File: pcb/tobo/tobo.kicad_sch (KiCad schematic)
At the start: 94 parts, among them J1 Molex 538-54548-2272, J2 Conn_01x02_Pin, J4 Molex 538-54548-2472, J5 Conn_01x09_Pin, J6 Conn_01x09_Pin, J7 Conn_01x09_Pin, J8 Hroparts Elec TYPE-C-31-M-12, U1 TS5A23167, U10 5015, U11 5015, U12 5015, U13 5015, U14 CH340E, U15 5015, U2 ATmega328P-A, U3 TS5A23167, U4 TS5A23167, U5 TS5A23167, U6 5015, U7 5015, U8 5015, U9 5015, X7 TestPoint, Y4 TestPoint

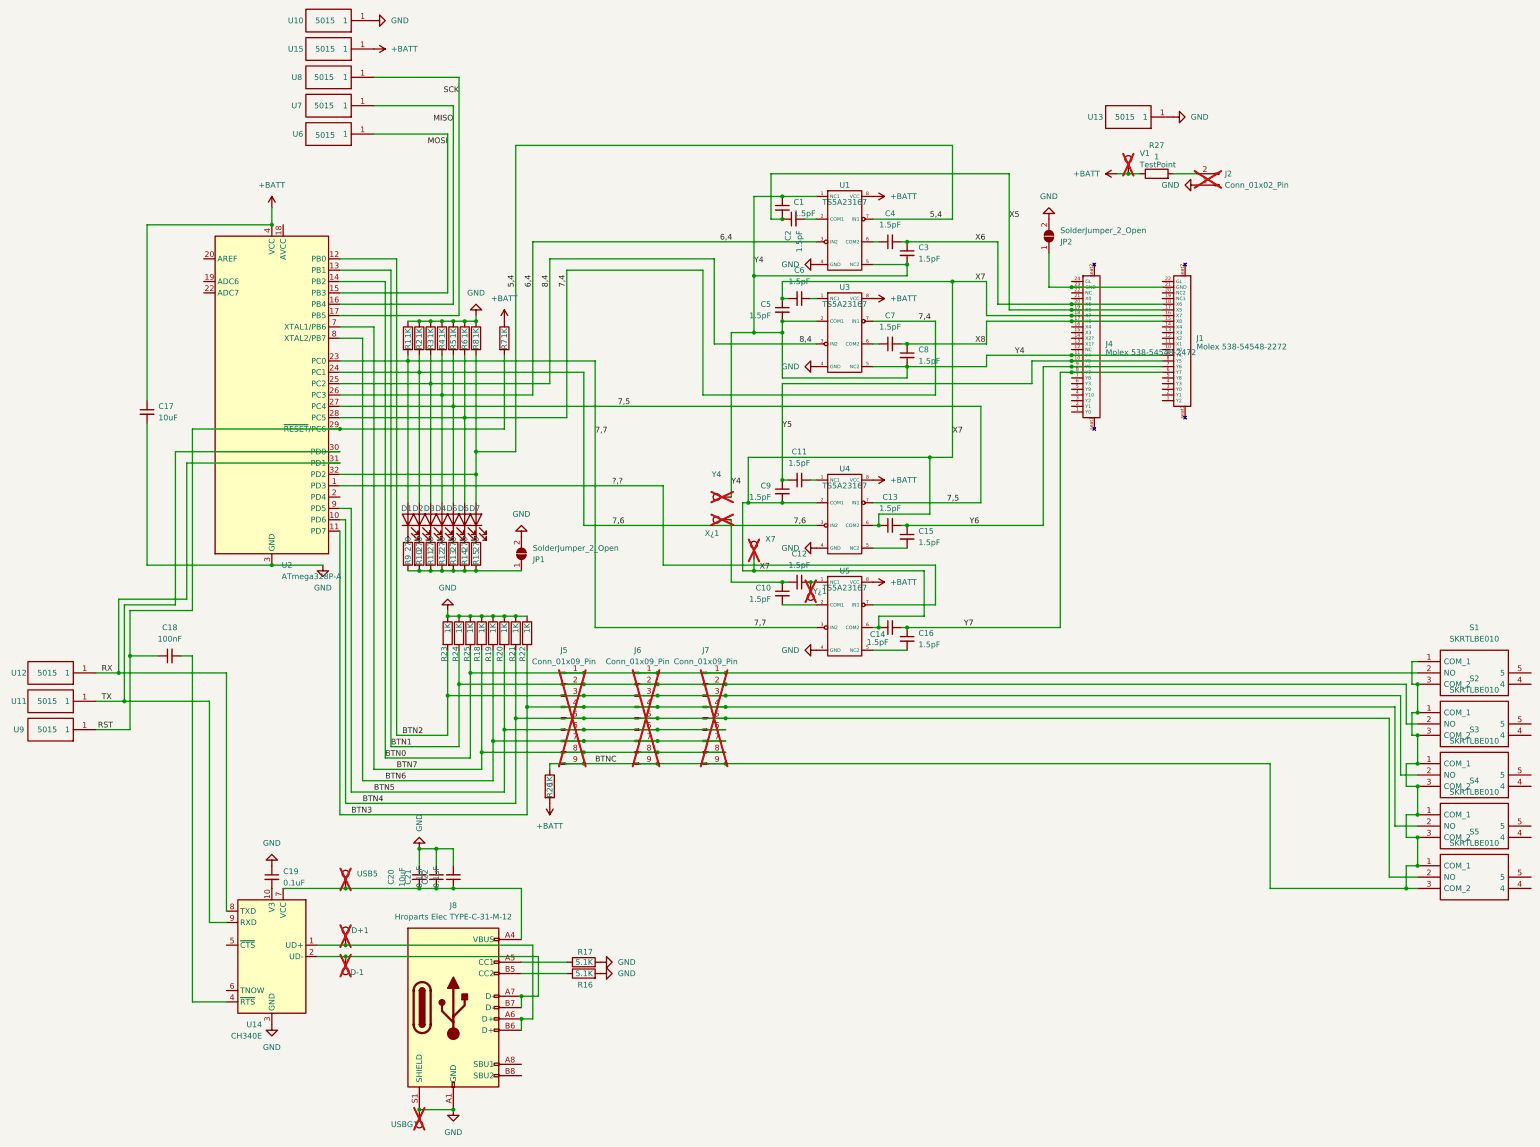
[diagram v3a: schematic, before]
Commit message: PCB cleanup, RST connector clarification
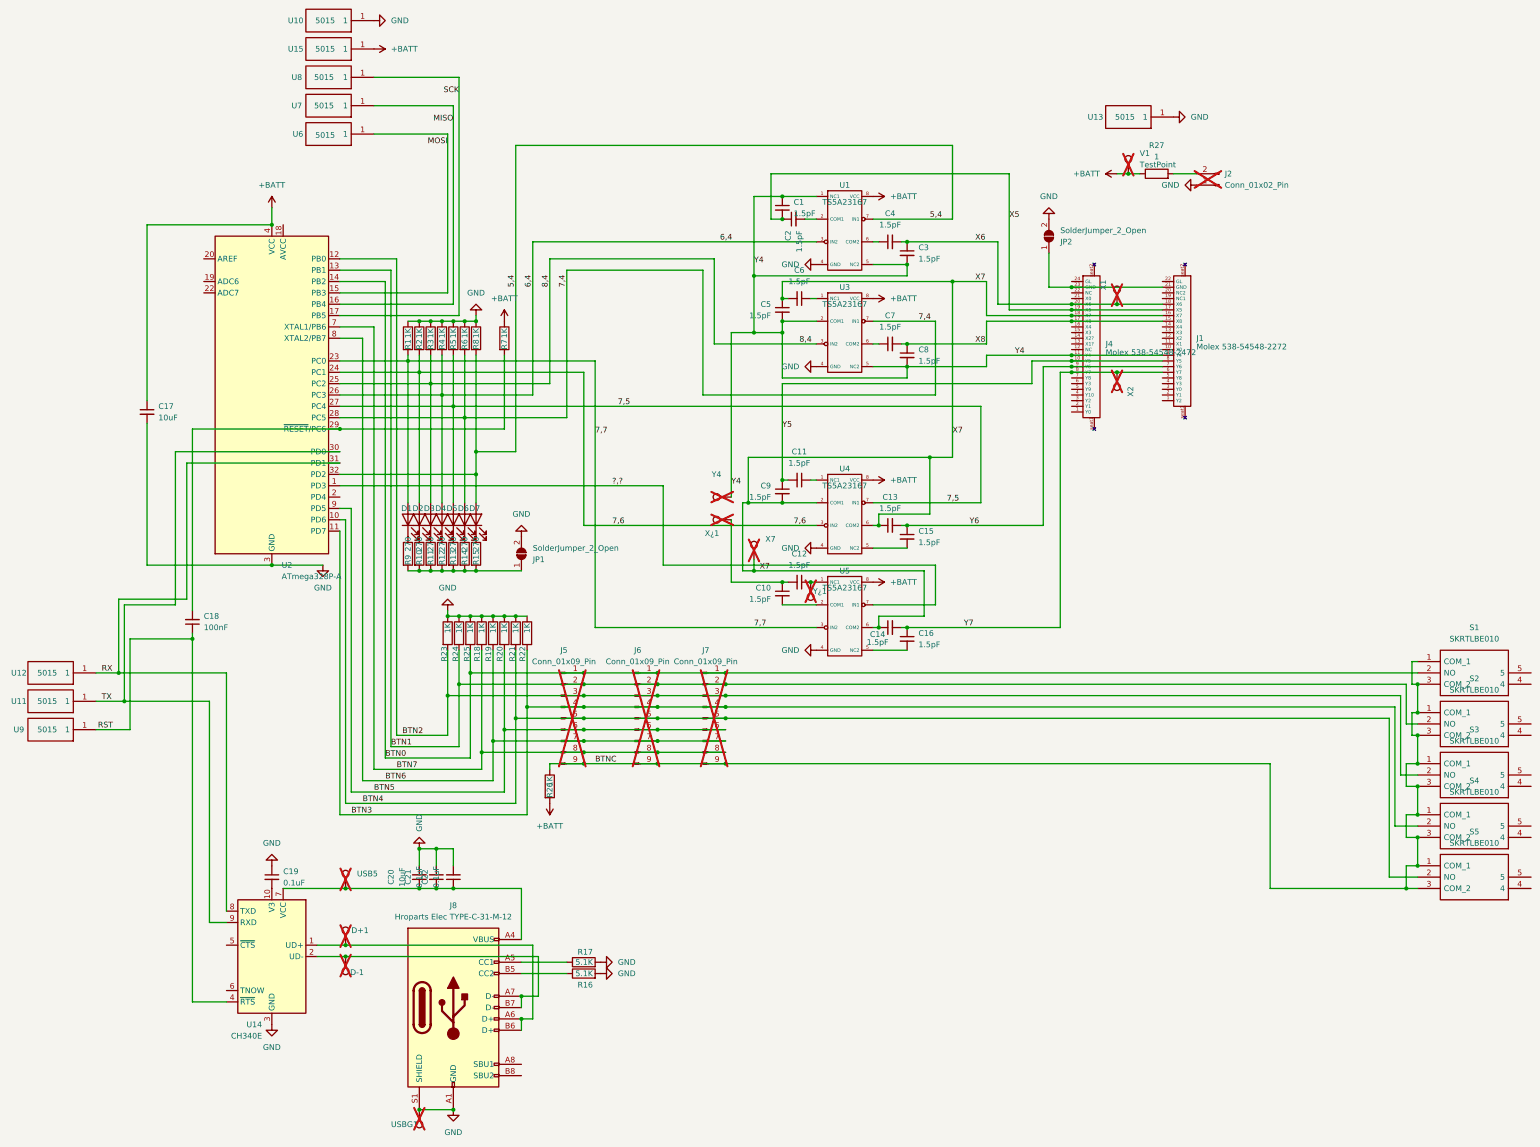
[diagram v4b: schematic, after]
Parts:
- added X1, X2: TestPoint, TestPoint:TestPoint_Pad_D1.0mm, symbol Connector:TestPoint
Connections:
- net RST: now also U14.4 (~{RTS}); no longer R7.2, U2.29 (~{RESET}/PC6)
- net X6: now also X1.1
- net Y7: now also X2.1
- net at C18.2: now also R7.2, U2.29 (~{RESET}/PC6); no longer U14.4 (~{RTS})
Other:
- moved on the sheet: C18
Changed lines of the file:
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@@
 	)
 	(junction
+		(at 264.16 97.79)
+		(diameter 0)
+		(color 0 0 0 0)
+	)
+	(junction
 		(at 176.53 175.26)
 		(diameter 0)
@@
 	)
 	(junction
-		(at 43.18 161.29)
-		(diameter 0)
-		(color 0 0 0 0)
-	)
-	(junction
 		(at 331.47 201.93)
 		(diameter 0)
@@
 	)
 	(junction
+		(at 57.15 157.48)
+		(diameter 0)
+		(color 0 0 0 0)
+	)
+	(junction
 		(at 130.81 237.49)
 		(diameter 0)
@@
 	)
 	(junction
+		(at 264.16 82.55)
+		(diameter 0)
+		(color 0 0 0 0)
+	)
+	(junction
 		(at 189.23 58.42)
 		(diameter 0)
@@
 	(wire
 		(pts
-			(xy 274.32 93.98) (xy 254 93.98)
-		)
-		(stroke
-			(width 0)
-			(type default)
-		)
-	)
-	(wire
-		(pts
-			(xy 43.18 161.29) (xy 43.18 177.8)
-		)
-		(stroke
-			(width 0)
-			(type default)
-		)
-	)
-	(wire
-		(pts
 			(xy 133.35 102.87) (xy 113.03 102.87)
 		)
@@
 	(wire
 		(pts
-			(xy 43.18 151.13) (xy 57.15 151.13)
-		)
-		(stroke
-			(width 0)
-			(type default)
-		)
-	)
-	(wire
-		(pts
 			(xy 328.93 176.53) (xy 331.47 176.53)
 		)
@@
 	(wire
 		(pts
+			(xy 264.16 82.55) (xy 254 82.55)
+		)
+		(stroke
+			(width 0)
+			(type default)
+		)
+	)
+	(wire
+		(pts
 			(xy 248.92 78.74) (xy 254 78.74)
 		)
@@
 	(wire
 		(pts
-			(xy 274.32 97.79) (xy 254 97.79)
+			(xy 274.32 97.79) (xy 264.16 97.79)
 		)
 		(stroke
@@
 	(wire
 		(pts
+			(xy 57.15 157.48) (xy 57.15 238.76)
+		)
+		(stroke
+			(width 0)
+			(type default)
+		)
+	)
+	(wire
+		(pts
 			(xy 130.81 242.57) (xy 133.35 242.57)
 		)
@@
 	(wire
 		(pts
-			(xy 274.32 82.55) (xy 254 82.55)
+			(xy 274.32 82.55) (xy 264.16 82.55)
 		)
 		(stroke
@@
 	(wire
 		(pts
+			(xy 43.18 157.48) (xy 57.15 157.48)
+		)
+		(stroke
+			(width 0)
+			(type default)
+		)
+	)
+	(wire
+		(pts
 			(xy 90.17 90.17) (xy 95.25 90.17)
 		)
@@
 	(wire
 		(pts
+			(xy 254 93.98) (xy 274.32 93.98)
+		)
+		(stroke
+			(width 0)
+			(type default)
+		)
+	)
+	(wire
+		(pts
 			(xy 107.95 208.28) (xy 107.95 204.47)
 		)
@@
 	(wire
 		(pts
+			(xy 43.18 157.48) (xy 43.18 177.8)
+		)
+		(stroke
+			(width 0)
+			(type default)
+		)
+	)
+	(wire
+		(pts
 			(xy 120.65 120.65) (xy 120.65 115.57)
 		)
@@
 	(wire
 		(pts
-			(xy 43.18 161.29) (xy 49.53 161.29)
-		)
-		(stroke
-			(width 0)
-			(type default)
-		)
-	)
-	(wire
-		(pts
-			(xy 57.15 161.29) (xy 57.15 238.76)
+			(xy 57.15 156.21) (xy 57.15 157.48)
 		)
 		(stroke
@@
 	(wire
 		(pts
-			(xy 57.15 161.29) (xy 54.61 161.29)
-		)
-		(stroke
-			(width 0)
-			(type default)
-		)
-	)
-	(wire
-		(pts
 			(xy 120.65 142.24) (xy 130.81 142.24)
 		)
@@
 	(wire
 		(pts
-			(xy 43.18 151.13) (xy 43.18 161.29)
+			(xy 189.23 121.92) (xy 190.5 121.92)
 		)
 		(stroke
@@
 	(wire
 		(pts
-			(xy 189.23 121.92) (xy 190.5 121.92)
+			(xy 264.16 53.34) (xy 266.7 53.34)
 		)
 		(stroke
@@
 	(wire
 		(pts
-			(xy 264.16 53.34) (xy 266.7 53.34)
+			(xy 227.33 77.47) (xy 234.95 77.47)
 		)
 		(stroke
@@
 	(wire
 		(pts
-			(xy 227.33 77.47) (xy 234.95 77.47)
+			(xy 245.11 95.25) (xy 245.11 100.33)
 		)
 		(stroke
@@
 	(wire
 		(pts
-			(xy 245.11 95.25) (xy 245.11 100.33)
+			(xy 274.32 96.52) (xy 254 96.52)
 		)
 		(stroke
@@
 	(wire
 		(pts
-			(xy 274.32 96.52) (xy 254 96.52)
+			(xy 140.97 74.93) (xy 140.97 107.95)
 		)
 		(stroke
@@
 	(wire
 		(pts
-			(xy 140.97 74.93) (xy 140.97 107.95)
+			(xy 264.16 97.79) (xy 254 97.79)
 		)
 		(stroke
@@
 	)
 	(symbol
+		(lib_id "Connector:TestPoint")
+		(at 264.16 97.79 180)
+		(unit 1)
+		(exclude_from_sim no)
+		(in_bom no)
+		(on_board yes)
+		(dnp yes)
+		(property "Reference" "X2"
+			(at 267.208 102.108 90)
+			(effects
+				(font
+					(size 1.27 1.27)
+				)
+			)
+		)
+		(property "Value" "TestPoint"
+			(at 261.62 101.092 90)
+			(effects
+				(font
+					(size 1.27 1.27)
+				)
+				(hide yes)
+			)
+		)
+		(property "Footprint" "TestPoint:TestPoint_Pad_D1.0mm"
+			(at 259.08 97.79 0)
+			(effects
+				(font
+					(size 1.27 1.27)
+				)
+				(hide yes)
+			)
+		)
+		(property "Datasheet" "~"
+			(at 259.08 97.79 0)
+			(effects
+				(font
+					(size 1.27 1.27)
+				)
+				(hide yes)
+			)
+		)
+		(property "Description" "test point"
+			(at 264.16 97.79 0)
+			(effects
+				(font
+					(size 1.27 1.27)
+				)
+				(hide yes)
+			)
+		)
+		(pin "1"
+		)
+		(instances
+			(project "tobo"
+				(path "/ce2fc4a9-618f-4cc1-898a-224ffa79d770"
+					(reference "X2")
+					(unit 1)
+				)
+			)
+		)
+	)
+	(symbol
 		(lib_id "Device:R")
 		(at 110.49 138.43 0)
@@
 	(symbol
 		(lib_id "Device:C_Small")
-		(at 52.07 161.29 90)
+		(at 57.15 153.67 180)
 		(unit 1)
 		(exclude_from_sim no)
@@
 		(fields_autoplaced yes)
 		(property "Reference" "C18"
-			(at 52.0763 154.94 90)
+			(at 59.69 152.3935 0)
 			(effects
 				(font
 					(size 1.27 1.27)
 				)
+				(justify right)
 			)
 		)
 		(property "Value" "100nF"
-			(at 52.0763 157.48 90)
+			(at 59.69 154.9335 0)
 			(effects
 				(font
 					(size 1.27 1.27)
 				)
+				(justify right)
 			)
 		)
 		(property "Footprint" "Capacitor_SMD:C_0201_0603Metric"
-			(at 52.07 161.29 0)
+			(at 57.15 153.67 0)
 			(effects
 				(font
@@
 		)
 		(property "Datasheet" "~"
-			(at 52.07 161.29 0)
+			(at 57.15 153.67 0)
 			(effects
 				(font
@@
 		)
 		(property "Description" "Unpolarized capacitor, small symbol"
-			(at 52.07 161.29 0)
+			(at 57.15 153.67 0)
 			(effects
 				(font
@@
 					(unit 1)
 				)
+			)
+		)
+	)
+	(symbol
+		(lib_id "Connector:TestPoint")
+		(at 264.16 82.55 0)
+		(unit 1)
+		(exclude_from_sim no)
+		(in_bom no)
+		(on_board yes)
+		(dnp yes)
+		(property "Reference" "X1"
+			(at 261.112 78.232 90)
+			(effects
+				(font
+					(size 1.27 1.27)
+				)
+			)
+		)
+		(property "Value" "TestPoint"
+			(at 266.7 79.248 90)
+			(effects
+				(font
+					(size 1.27 1.27)
+				)
+				(hide yes)
+			)
+		)
+		(property "Footprint" "TestPoint:TestPoint_Pad_D1.0mm"
+			(at 269.24 82.55 0)
+			(effects
+				(font
+					(size 1.27 1.27)
+				)
+				(hide yes)
+			)
+		)
+		(property "Datasheet" "~"
+			(at 269.24 82.55 0)
+			(effects
+				(font
+					(size 1.27 1.27)
+				)
+				(hide yes)
+			)
+		)
+		(property "Description" "test point"
+			(at 264.16 82.55 0)
+			(effects
+				(font
+					(size 1.27 1.27)
+				)
+				(hide yes)
+			)
+		)
+		(pin "1"
+		)
+		(instances
+			(project "tobo"
+				(path "/ce2fc4a9-618f-4cc1-898a-224ffa79d770"
+					(reference "X1")
+					(unit 1)
+				)
